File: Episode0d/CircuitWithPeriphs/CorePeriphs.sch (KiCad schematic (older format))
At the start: 2 parts, among them U301 82C55A

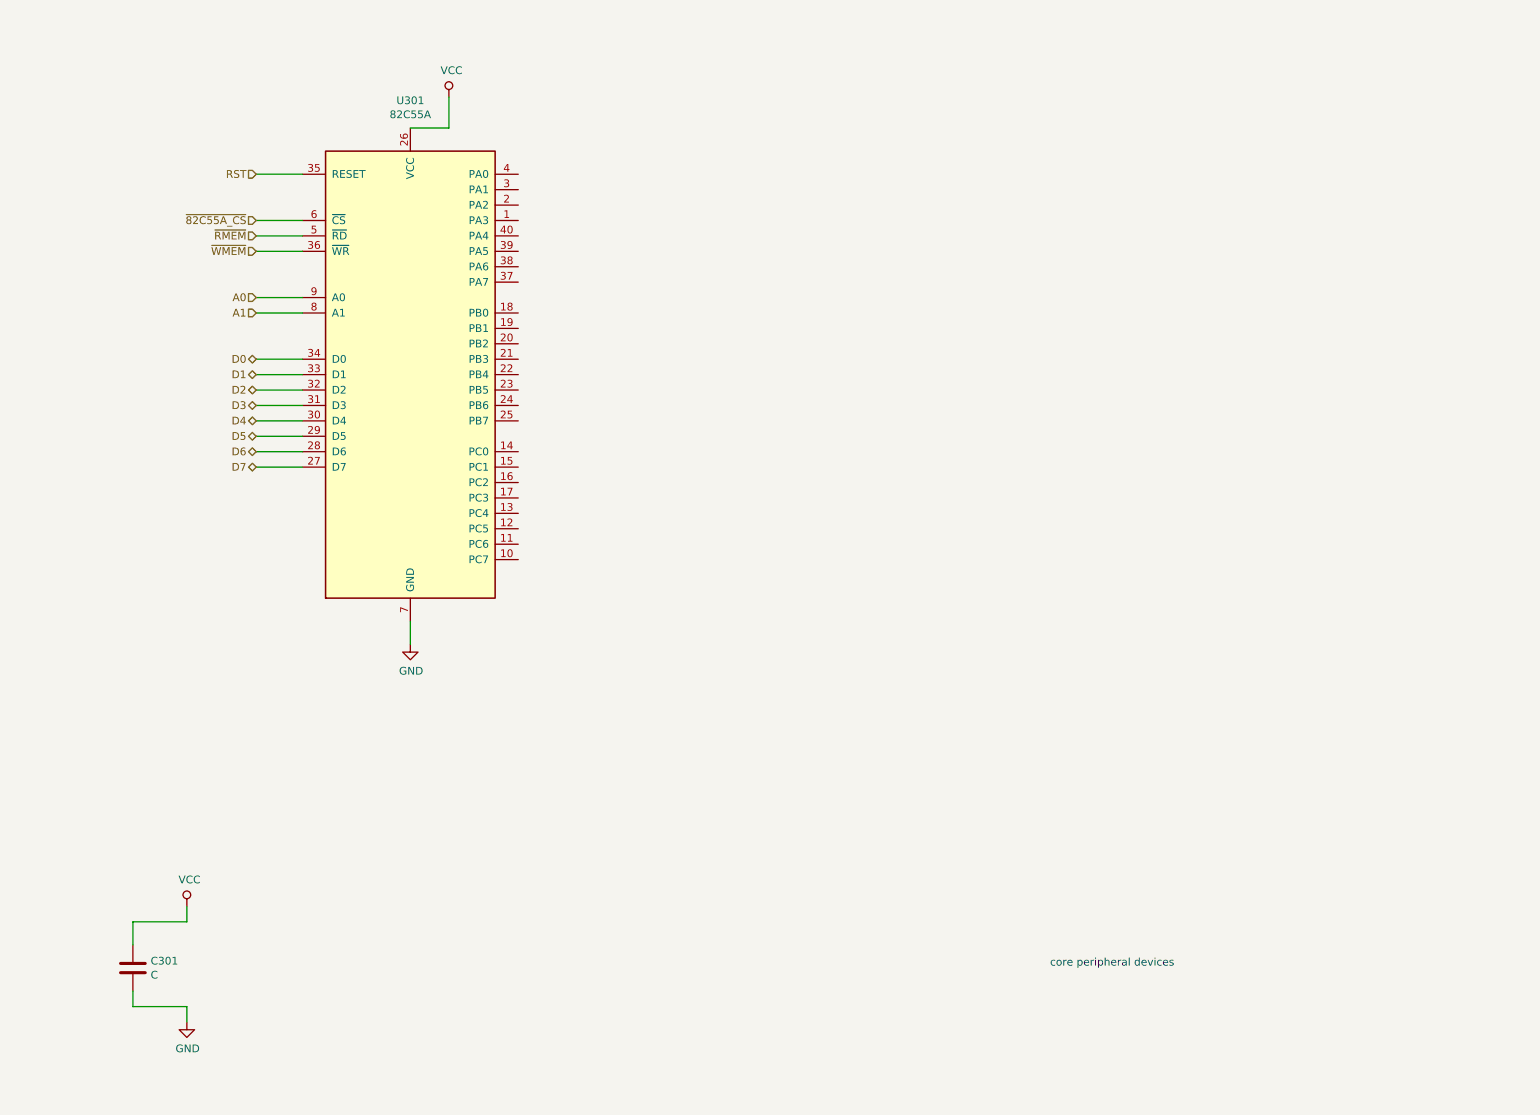
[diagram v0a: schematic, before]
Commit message: added i82c54, various schematic cleanups
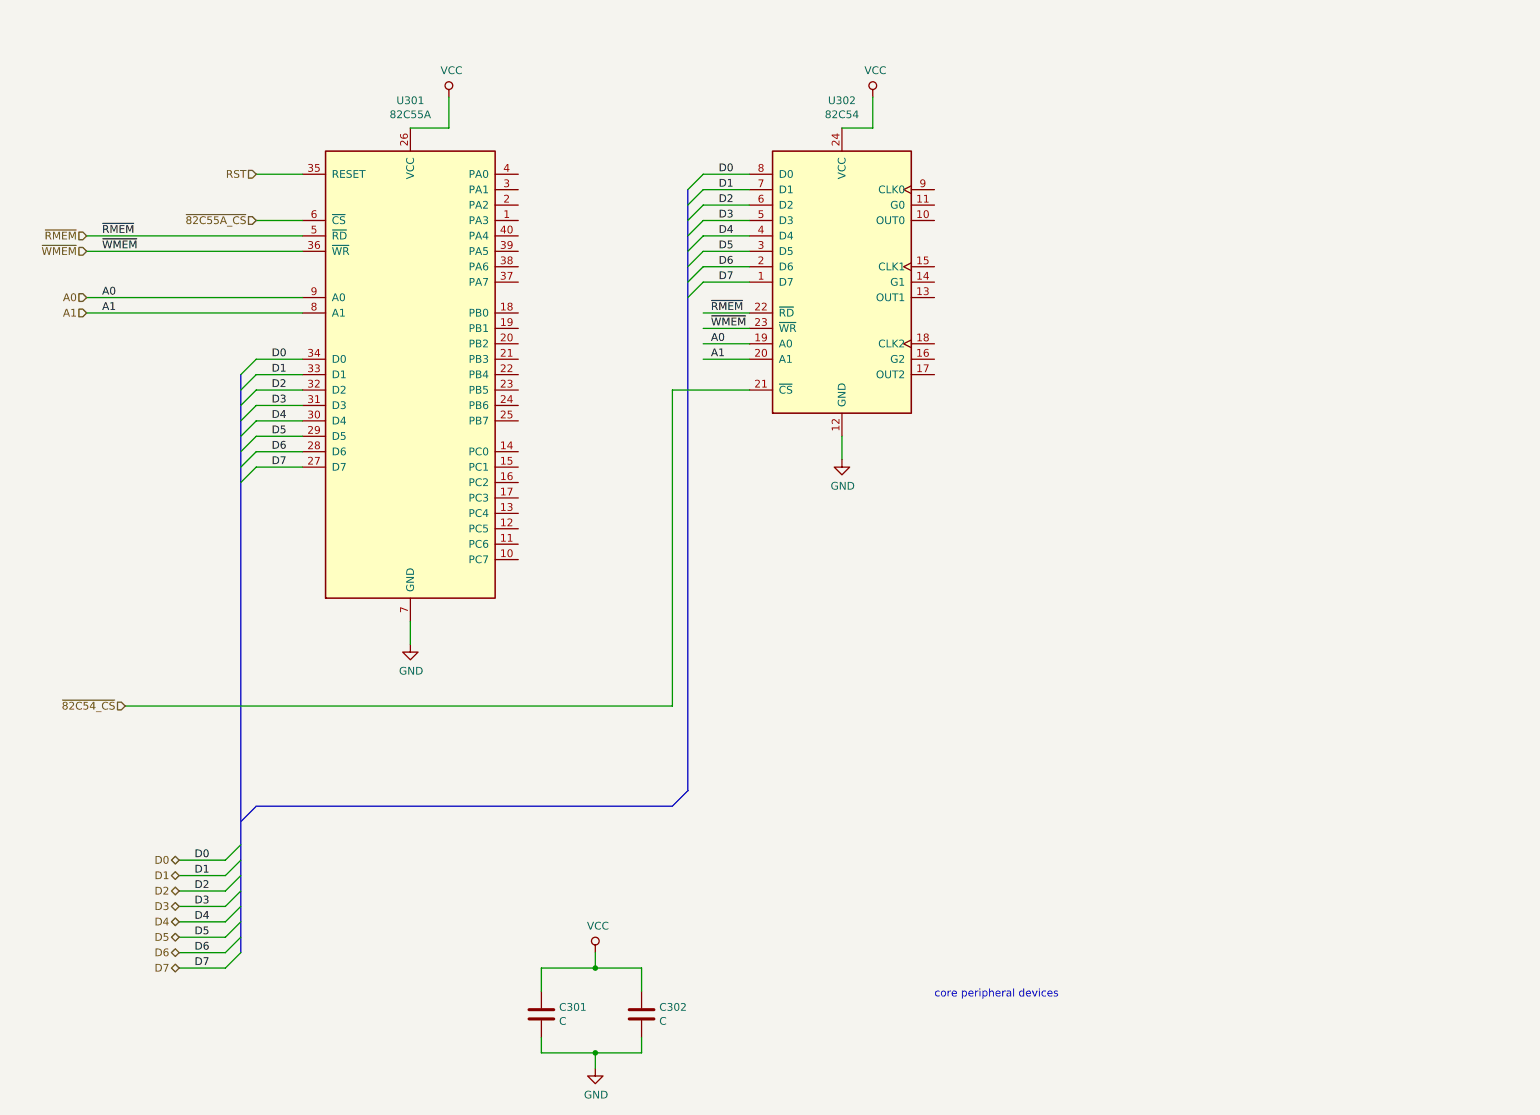
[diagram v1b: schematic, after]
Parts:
- added C302: C, symbol device:C
- added U302: 82C54, Housings_DIP:DIP-24_W15.24mm, symbol intel:82C54
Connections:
- net labels added: ~82C54_CS
- wire segments 23 -> 53
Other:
- moved on the sheet: C301

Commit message: use E signal as timer input for 82c54
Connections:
- net labels added: E
- wire segments 53 -> 69
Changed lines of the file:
@@
 	4450 7300 4150 7300
 Connection ~ 4150 7300
+Wire Wire Line
+	6350 2800 6500 2800
+Wire Wire Line
+	6500 2800 6500 2300
+$Comp
+L power:VCC #PWR?
+U 1 1 5DE3C94B
+P 6500 1100
+F 0 "#PWR?" H 6500 950 50  0001 C CNN
+F 1 "VCC" H 6517 1273 50  0000 C CNN
+F 2 "" H 6500 1100 50  0001 C CNN
+F 3 "" H 6500 1100 50  0001 C CNN
+	1    6500 1100
+	1    0    0    -1
+$EndComp
+Wire Wire Line
+	6350 1800 6500 1800
+Connection ~ 6500 1800
+Wire Wire Line
+	6500 1800 6500 1100
+Wire Wire Line
+	6350 2300 6500 2300
+Connection ~ 6500 2300
+Wire Wire Line
+	6500 2300 6500 1800
+Text HLabel 6100 700  0    50   Input ~ 0
+E
+Wire Wire Line
+	6350 2700 6600 2700
+Wire Wire Line
+	6600 2700 6600 2200
+Wire Wire Line
+	6600 700  6100 700
+Wire Wire Line
+	6350 1700 6600 1700
+Connection ~ 6600 1700
+Wire Wire Line
+	6600 1700 6600 700
+Wire Wire Line
+	6350 2200 6600 2200
+Connection ~ 6600 2200
+Wire Wire Line
+	6600 2200 6600 1700
+Wire Wire Line
+	6350 1900 7000 1900
+Wire Wire Line
+	6350 2400 7000 2400
+Wire Wire Line
+	6350 2900 7000 2900
 Wire Bus Line
 	4750 1700 4750 5600

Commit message: working on integrating ACIA device
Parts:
- added C303: C, symbol device:C
- added U303: MC6850, MODULE, symbol MC6850:MC6850
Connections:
- net labels added: R~W, ~6850_CS
- wire segments 69 -> 106
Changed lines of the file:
@@
 Entry Bus Bus
 	4650 5700 4750 5600
-Wire Bus Line
-	4650 5700 1950 5700
 Wire Wire Line
 	5150 2500 4850 2500
@@
 	6600 2200 6600 1700
 Wire Wire Line
-	6350 1900 7000 1900
-Wire Wire Line
 	6350 2400 7000 2400
 Wire Wire Line
 	6350 2900 7000 2900
+$Comp
+L MC6850:MC6850 U303
+U 1 1 5DE258A4
+P 8750 2200
+F 0 "U303" H 8750 3115 50  0000 C CNN
+F 1 "MC6850" H 8750 3024 50  0000 C CNN
+F 2 "MODULE" H 8750 2200 50  0001 C CNN
+F 3 "DOCUMENTATION" H 8750 2200 50  0001 C CNN
+	1    8750 2200
+	1    0    0    -1
+$EndComp
+Wire Wire Line
+	8000 2750 7900 2750
+Wire Wire Line
+	7900 2750 7900 3300
+Wire Wire Line
+	7900 3300 7750 3300
+Wire Wire Line
+	7750 3300 7750 3200
+$Comp
+L power:VCC #PWR?
+U 1 1 5DE28823
+P 7750 3200
+F 0 "#PWR?" H 7750 3050 50  0001 C CNN
+F 1 "VCC" H 7767 3373 50  0000 C CNN
+F 2 "" H 7750 3200 50  0001 C CNN
+F 3 "" H 7750 3200 50  0001 C CNN
+	1    7750 3200
+	1    0    0    -1
+$EndComp
+Wire Wire Line
+	8000 1650 7900 1650
+Wire Wire Line
+	7900 1650 7900 1150
+Wire Wire Line
+	7900 1150 7750 1150
+Wire Wire Line
+	7750 1150 7750 1250
+$Comp
+L power:GND #PWR?
+U 1 1 5DE2A229
+P 7750 1250
+F 0 "#PWR?" H 7750 1000 50  0001 C CNN
+F 1 "GND" H 7755 1077 50  0000 C CNN
+F 2 "" H 7750 1250 50  0001 C CNN
+F 3 "" H 7750 1250 50  0001 C CNN
+	1    7750 1250
+	1    0    0    -1
+$EndComp
+Wire Wire Line
+	9500 1850 10100 1850
+Wire Wire Line
+	9500 1950 10100 1950
+Wire Wire Line
+	9500 2050 10100 2050
+Wire Wire Line
+	9500 2150 10100 2150
+Wire Wire Line
+	9500 2250 10100 2250
+Wire Wire Line
+	9500 2350 10100 2350
+Wire Wire Line
+	9500 2450 10100 2450
+Wire Wire Line
+	9500 2550 10100 2550
+Text Label 9900 1850 0    50   ~ 0
+D0
+Text Label 9900 1950 0    50   ~ 0
+D1
+Text Label 9900 2050 0    50   ~ 0
+D2
+Text Label 9900 2150 0    50   ~ 0
+D3
+Text Label 9900 2250 0    50   ~ 0
+D4
+Text Label 9900 2350 0    50   ~ 0
+D5
+Text Label 9900 2450 0    50   ~ 0
+D6
+Text Label 9900 2550 0    50   ~ 0
+D7
+Entry Wire Line
+	10100 1850 10200 1950
+Entry Wire Line
+	10100 1950 10200 2050
+Entry Wire Line
+	10100 2050 10200 2150
+Entry Wire Line
+	10100 2150 10200 2250
+Entry Wire Line
+	10100 2250 10200 2350
+Entry Wire Line
+	10100 2350 10200 2450
+Entry Wire Line
+	10100 2450 10200 2550
+Entry Wire Line
+	10100 2550 10200 2650
+Wire Wire Line
+	9500 2650 9600 2650
+Wire Wire Line
+	9600 2650 9600 700
+Wire Wire Line
+	9600 700  6600 700
+Connection ~ 6600 700
+Text HLabel 6100 600  0    50   Input ~ 0
+R~W
+Wire Wire Line
+	9500 2750 9700 2750
+Wire Wire Line
+	9700 2750 9700 600
+Wire Wire Line
+	9700 600  6100 600
+Wire Wire Line
+	7900 1900 7900 1850
+Wire Wire Line
+	7900 1850 8000 1850
+Wire Wire Line
+	6350 1900 7900 1900
+Wire Wire Line
+	8000 1950 7900 1950
+Wire Wire Line
+	7900 1950 7900 1900
+Connection ~ 7900 1900
+Text HLabel 1100 5150 0    50   Input ~ 0
+~6850_CS
+Wire Wire Line
+	1100 5150 7550 5150
+Wire Wire Line
+	7550 5150 7550 2450
+Wire Wire Line
+	7550 2450 8000 2450
+Wire Wire Line
+	8000 2350 7900 2350
+Wire Wire Line
+	7900 2350 7900 2550
+Connection ~ 7900 2750
+Wire Wire Line
+	8000 2550 7900 2550
+Connection ~ 7900 2550
+Wire Wire Line
+	7900 2550 7900 2750
+$Comp
+L device:C C303
+U 1 1 5DEAC8D1
+P 4950 7050
+F 0 "C303" H 5065 7096 50  0000 L CNN
+F 1 "C" H 5065 7005 50  0000 L CNN
+F 2 "" H 4988 6900 50  0001 C CNN
+F 3 "" H 4950 7050 50  0001 C CNN
+	1    4950 7050
+	1    0    0    -1
+$EndComp
+Wire Wire Line
+	4950 6900 4950 6750
+Wire Wire Line
+	4950 7200 4950 7300
+Wire Wire Line
+	4950 6750 4450 6750
+Connection ~ 4450 6750
+Wire Wire Line
+	4950 7300 4450 7300
+Wire Bus Line
+	1950 5700 10200 5700
+Wire Bus Line
+	10200 1950 10200 5700
 Wire Bus Line
 	4750 1700 4750 5600
 Wire Bus Line
 	1850 2900 1850 6650
+Connection ~ 4450 7300
 $EndSCHEMATC
